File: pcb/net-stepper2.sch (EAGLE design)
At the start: 37 parts, among them J1 MICRO-USB, J2 POWER_JACKPTH_LOCK, J3 ENCODER, J4 ENDSTOP2, J5 ENDSTOP1, J6 STEPER, Q1 600mA/40V, Q2 600mA/40V, U1 L6470, U2 CP2104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

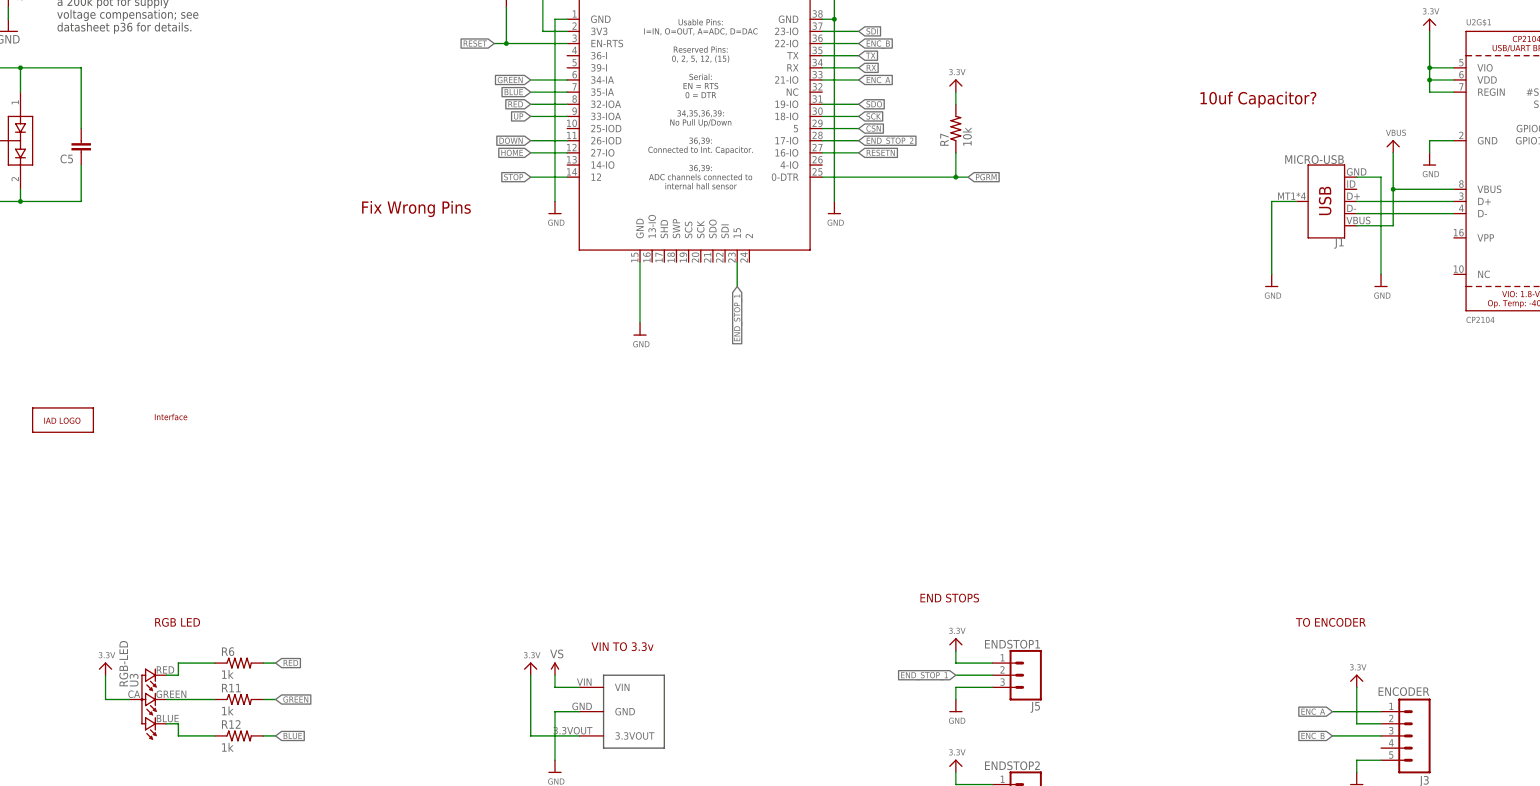
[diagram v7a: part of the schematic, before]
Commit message: added capacitor
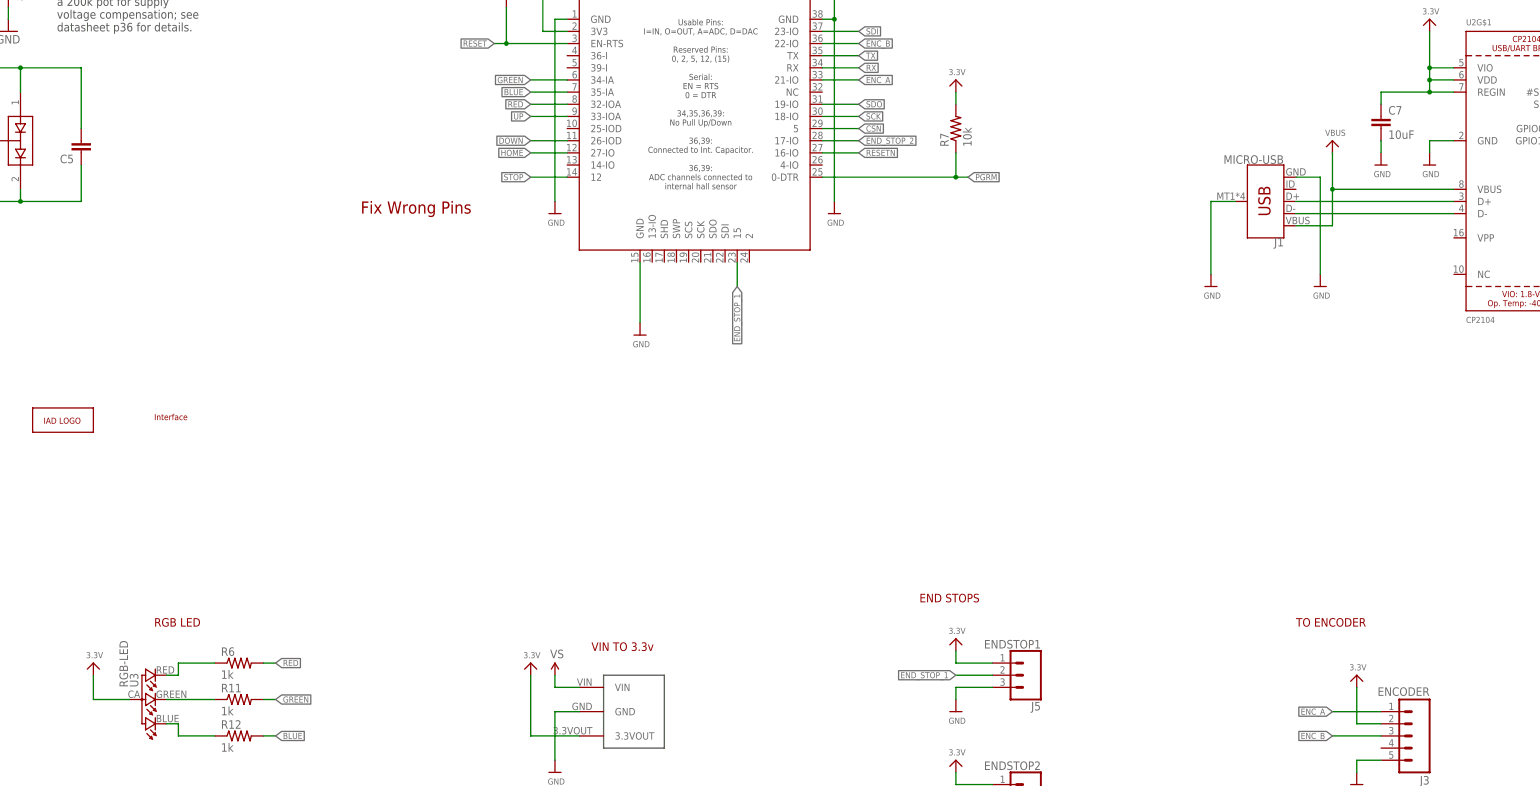
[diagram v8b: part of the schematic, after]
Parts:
- added C7: 10uF, SparkFun-Capacitors:10UF-0603-6.3V-20%
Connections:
- net 3.3V: now also C7.1
- net GND: now also C7.2
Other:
- note removed: "10uf Capacitor?"
- moved on the sheet: J1
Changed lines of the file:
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@@
 <part name="GND4" library="SparkFun" deviceset="GND" device=""/>
 <part name="P+4" library="SparkFun-Aesthetics" deviceset="3.3V" device=""/>
+<part name="C7" library="SparkFun-Capacitors" deviceset="10UF" device="-0603-6.3V-20%" value="10uF"/>
+<part name="U$18" library="microbuilder" deviceset="GND" device=""/>
 </parts>
 <sheets>
@@
 <text x="474.98" y="157.48" size="1.778" layer="94">USB TO SERIAL CONVERTER</text>
 <text x="205.74" y="25.4" size="1.778" layer="94">RGB LED</text>
-<text x="424.18" y="134.62" size="2.54" layer="94" font="vector" ratio="20">10uf Capacitor?</text>
 <text x="248.92" y="111.76" size="2.54" layer="94" font="vector" ratio="20">Fix Wrong Pins</text>
 </plain>
@@
 <instance part="S4" gate="G$1" x="134.62" y="-2.54"/>
 <instance part="S3" gate="G$1" x="134.62" y="7.62"/>
-<instance part="U$33" gate="G$1" x="462.28" y="96.52"/>
+<instance part="U$33" gate="G$1" x="449.58" y="96.52"/>
 <instance part="U$34" gate="G$1" x="472.44" y="121.92"/>
-<instance part="U$36" gate="G$1" x="464.82" y="127"/>
+<instance part="U$36" gate="G$1" x="452.12" y="127"/>
 <instance part="U$38" gate="G$1" x="472.44" y="152.4"/>
-<instance part="J1" gate="G$1" x="452.12" y="114.3" rot="R180"/>
+<instance part="J1" gate="G$1" x="439.42" y="114.3" rot="R180"/>
 <instance part="U3" gate="G$1" x="203.2" y="10.16" rot="R90"/>
-<instance part="U$26" gate="G$1" x="195.58" y="17.78"/>
+<instance part="U$26" gate="G$1" x="193.04" y="17.78"/>
 <instance part="R6" gate="G$1" x="223.52" y="17.78"/>
 <instance part="R11" gate="G$1" x="223.52" y="10.16"/>
@@
 <instance part="P+3" gate="G$1" x="109.22" y="185.42"/>
 <instance part="GND1" gate="1" x="30.48" y="0"/>
-<instance part="U$7" gate="G$1" x="439.42" y="96.52"/>
+<instance part="U$7" gate="G$1" x="426.72" y="96.52"/>
 <instance part="U2" gate="G$1" x="492.76" y="121.92"/>
 <instance part="U2" gate="G$2" x="528.32" y="137.16"/>
@@
 <instance part="GND4" gate="1" x="139.7" y="91.44"/>
 <instance part="P+4" gate="G$1" x="152.4" y="109.22"/>
+<instance part="C7" gate="G$1" x="462.28" y="129.54"/>
+<instance part="U$18" gate="G$1" x="462.28" y="121.92"/>
 </instances>
 <busses>
@@
 <pinref part="U$33" gate="G$1" pin="GND"/>
 <pinref part="J1" gate="G$1" pin="GND"/>
-<wire x1="457.2" y1="119.38" x2="462.28" y2="119.38" width="0.1524" layer="91"/>
-<wire x1="462.28" y1="119.38" x2="462.28" y2="99.06" width="0.1524" layer="91"/>
+<wire x1="444.5" y1="119.38" x2="449.58" y2="119.38" width="0.1524" layer="91"/>
+<wire x1="449.58" y1="119.38" x2="449.58" y2="99.06" width="0.1524" layer="91"/>
 </segment>
 <segment>
@@
 <segment>
 <pinref part="J1" gate="G$1" pin="SHIELD"/>
-<wire x1="444.5" y1="114.3" x2="439.42" y2="114.3" width="0.1524" layer="91"/>
+<wire x1="431.8" y1="114.3" x2="426.72" y2="114.3" width="0.1524" layer="91"/>
 <pinref part="U$7" gate="G$1" pin="GND"/>
-<wire x1="439.42" y1="99.06" x2="439.42" y2="114.3" width="0.1524" layer="91"/>
+<wire x1="426.72" y1="99.06" x2="426.72" y2="114.3" width="0.1524" layer="91"/>
 </segment>
 <segment>
@@
 <pinref part="U2" gate="G$2" pin="TP"/>
 <wire x1="528.32" y1="124.46" x2="528.32" y2="129.54" width="0.1524" layer="91"/>
+</segment>
+<segment>
+<pinref part="U$18" gate="G$1" pin="GND"/>
+<pinref part="C7" gate="G$1" pin="2"/>
+<wire x1="462.28" y1="124.46" x2="462.28" y2="127" width="0.1524" layer="91"/>
 </segment>
 </net>
@@
 <junction x="472.44" y="142.24"/>
 <wire x1="472.44" y1="139.7" x2="472.44" y2="137.16" width="0.1524" layer="91"/>
+<pinref part="C7" gate="G$1" pin="1"/>
+<wire x1="472.44" y1="137.16" x2="462.28" y2="137.16" width="0.1524" layer="91"/>
+<wire x1="462.28" y1="137.16" x2="462.28" y2="134.62" width="0.1524" layer="91"/>
+<junction x="472.44" y="137.16"/>
 </segment>
 <segment>
 <pinref part="U3" gate="G$1" pin="1"/>
-<wire x1="200.66" y1="10.16" x2="195.58" y2="10.16" width="0.1524" layer="91"/>
+<wire x1="200.66" y1="10.16" x2="193.04" y2="10.16" width="0.1524" layer="91"/>
 <pinref part="U$26" gate="G$1" pin="3.3V"/>
-<wire x1="195.58" y1="10.16" x2="195.58" y2="15.24" width="0.1524" layer="91"/>
+<wire x1="193.04" y1="10.16" x2="193.04" y2="15.24" width="0.1524" layer="91"/>
 </segment>
 </net>
@@
 <net name="VBUS" class="0">
 <segment>
-<wire x1="464.82" y1="116.84" x2="477.52" y2="116.84" width="0.1524" layer="91"/>
+<wire x1="452.12" y1="116.84" x2="477.52" y2="116.84" width="0.1524" layer="91"/>
 <pinref part="U$36" gate="G$1" pin="VBUS"/>
-<wire x1="464.82" y1="116.84" x2="464.82" y2="124.46" width="0.1524" layer="91"/>
+<wire x1="452.12" y1="116.84" x2="452.12" y2="124.46" width="0.1524" layer="91"/>
 <pinref part="J1" gate="G$1" pin="VBUS"/>
-<wire x1="457.2" y1="109.22" x2="464.82" y2="109.22" width="0.1524" layer="91"/>
-<wire x1="464.82" y1="109.22" x2="464.82" y2="116.84" width="0.1524" layer="91"/>
-<junction x="464.82" y="116.84"/>
+<wire x1="444.5" y1="109.22" x2="452.12" y2="109.22" width="0.1524" layer="91"/>
+<wire x1="452.12" y1="109.22" x2="452.12" y2="116.84" width="0.1524" layer="91"/>
+<junction x="452.12" y="116.84"/>
 <pinref part="U2" gate="G$1" pin="VBUS"/>
 </segment>
@@
 <segment>
 <pinref part="J1" gate="G$1" pin="D+"/>
-<wire x1="457.2" y1="114.3" x2="477.52" y2="114.3" width="0.1524" layer="91"/>
+<wire x1="444.5" y1="114.3" x2="477.52" y2="114.3" width="0.1524" layer="91"/>
 <pinref part="U2" gate="G$1" pin="D+"/>
 </segment>
@@
 <segment>
 <pinref part="J1" gate="G$1" pin="D-"/>
-<wire x1="457.2" y1="111.76" x2="477.52" y2="111.76" width="0.1524" layer="91"/>
+<wire x1="444.5" y1="111.76" x2="477.52" y2="111.76" width="0.1524" layer="91"/>
 <pinref part="U2" gate="G$1" pin="D-"/>
 </segment>
